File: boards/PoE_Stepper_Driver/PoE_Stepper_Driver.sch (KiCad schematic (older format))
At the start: 28 parts, among them SW3 SW_Push, U3 STM32F407VETx, U4 NCP1117, U5 E48SC12010, Y1 8MHz

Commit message: fixed ground issue
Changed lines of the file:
@@
 NoConn ~ 3225 5800
 NoConn ~ 5025 1600
-$Comp
-L ECE445:E48SC12010 U5
-U 1 1 62597F21
-P 9150 2175
-F 0 "U5" H 9475 2340 50  0000 C CNN
-F 1 "E48SC12010" H 9475 2249 50  0000 C CNN
-F 2 "PoE_Stepper_Driver:E48SC12010" H 9150 2175 50  0001 C CNN
-F 3 "" H 9150 2175 50  0001 C CNN
-	1    9150 2175
-	1    0    0    -1
-$EndComp
 Wire Wire Line
 	10050 2275 10075 2275
@@
 	10125 2275 10125 2250
 Connection ~ 10075 2275
+$Comp
+L ECE445:E48SC12010 U5
+U 1 1 62D0E6E4
+P 9150 2175
+F 0 "U5" H 9550 2340 50  0000 C CNN
+F 1 "E48SC12010" H 9550 2249 50  0000 C CNN
+F 2 "PoE_Stepper_Driver:E48SC12010" H 9150 2175 50  0001 C CNN
+F 3 "" H 9150 2175 50  0001 C CNN
+	1    9150 2175
+	1    0    0    -1
+$EndComp
 $EndSCHEMATC

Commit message: finished footprint assignment
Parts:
- removed C40: 2.2uF, symbol device:C_Small
- removed C41, C42: 2.2nF, symbol device:C_Small
- removed FL1: 1.32mH, symbol device:EMI_Filter_CommonMode
- C12, C6: value C_Small -> 20pF; footprint (none) -> Capacitor_SMD:C_0603_1608Metric_Pad1.05x0.95mm_HandSolder
- C40: renamed from C43; value 100uF -> 47uF; footprint (none) -> Capacitor_THT:CP_Radial_D8.0mm_P3.50mm
- C8, C9: footprint (none) -> Capacitor_SMD:CP_Elec_6.3x5.4
- R1, R2, R37: footprint (none) -> Resistor_SMD:R_0805_2012Metric_Pad1.15x1.40mm_HandSolder
- R3: value R_Small -> 220; footprint (none) -> Resistor_SMD:R_0603_1608Metric_Pad1.05x0.95mm_HandSolder
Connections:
- wire segments 135 -> 123
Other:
- moved on the sheet: C40, U5
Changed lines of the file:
@@
 F1 "Motor_Control.sch" 50
 $EndSheet
-Text GLabel 9050 2575 0    50   Input ~ 0
+Text GLabel 8375 2500 0    50   Input ~ 0
 PWRGD
-Text GLabel 6925 2475 0    50   Input ~ 0
+Text GLabel 7850 2275 0    50   Input ~ 0
 VOUT+
-Text GLabel 6925 2675 0    50   Input ~ 0
+Text GLabel 7850 2725 0    50   Input ~ 0
 VOUT-
 $Comp
@@
 L power:+12V #PWR014
 U 1 1 62158186
-P 10125 2250
-F 0 "#PWR014" H 10125 2100 50  0001 C CNN
-F 1 "+12V" H 10140 2423 50  0000 C CNN
-F 2 "" H 10125 2250 50  0001 C CNN
-F 3 "" H 10125 2250 50  0001 C CNN
-	1    10125 2250
+P 9450 2175
+F 0 "#PWR014" H 9450 2025 50  0001 C CNN
+F 1 "+12V" H 9465 2348 50  0000 C CNN
+F 2 "" H 9450 2175 50  0001 C CNN
+F 3 "" H 9450 2175 50  0001 C CNN
+	1    9450 2175
 	1    0    0    -1
 $EndComp
@@
 L power:GND #PWR015
 U 1 1 6215A31C
-P 10125 2900
-F 0 "#PWR015" H 10125 2650 50  0001 C CNN
-F 1 "GND" H 10130 2727 50  0000 C CNN
-F 2 "" H 10125 2900 50  0001 C CNN
-F 3 "" H 10125 2900 50  0001 C CNN
-	1    10125 2900
+P 9450 2825
+F 0 "#PWR015" H 9450 2575 50  0001 C CNN
+F 1 "GND" H 9455 2652 50  0000 C CNN
+F 2 "" H 9450 2825 50  0001 C CNN
+F 3 "" H 9450 2825 50  0001 C CNN
+	1    9450 2825
 	1    0    0    -1
 $EndComp
@@
 F 0 "C9" H 9091 4171 50  0000 L CNN
 F 1 "10uF" H 9091 4080 50  0000 L CNN
-F 2 "" H 9000 4125 50  0001 C CNN
+F 2 "Capacitor_SMD:CP_Elec_6.3x5.4" H 9000 4125 50  0001 C CNN
 F 3 "~" H 9000 4125 50  0001 C CNN
 	1    9000 4125
@@
 F 0 "C8" H 7875 4150 50  0000 L CNN
 F 1 "10uF" H 7800 4075 50  0000 L CNN
-F 2 "" H 8075 4125 50  0001 C CNN
+F 2 "Capacitor_SMD:CP_Elec_6.3x5.4" H 8075 4125 50  0001 C CNN
 F 3 "~" H 8075 4125 50  0001 C CNN
 	1    8075 4125
 	1    0    0    -1
 $EndComp
-Text Notes 8400 2125 0    50   ~ 10
+Text Notes 7725 2050 0    50   ~ 10
 Power
 $Comp
@@
 P 3000 3000
 F 0 "R3" V 3100 3000 50  0000 C CNN
-F 1 "R_Small" V 3175 3000 50  0000 C CNN
-F 2 "" H 3000 3000 50  0001 C CNN
+F 1 "220" V 3175 3000 50  0000 C CNN
+F 2 "Resistor_SMD:R_0603_1608Metric_Pad1.05x0.95mm_HandSolder" H 3000 3000 50  0001 C CNN
 F 3 "~" H 3000 3000 50  0001 C CNN
 	1    3000 3000
@@
 P 2525 2725
 F 0 "C12" V 2296 2725 50  0000 C CNN
-F 1 "C_Small" V 2387 2725 50  0000 C CNN
-F 2 "" H 2525 2725 50  0001 C CNN
+F 1 "20pF" V 2387 2725 50  0000 C CNN
+F 2 "Capacitor_SMD:C_0603_1608Metric_Pad1.05x0.95mm_HandSolder" H 2525 2725 50  0001 C CNN
 F 3 "~" H 2525 2725 50  0001 C CNN
 	1    2525 2725
@@
 P 2525 3000
 F 0 "C6" V 2650 3000 50  0000 C CNN
-F 1 "C_Small" V 2725 3000 50  0000 C CNN
-F 2 "" H 2525 3000 50  0001 C CNN
+F 1 "20pF" V 2725 3000 50  0000 C CNN
+F 2 "Capacitor_SMD:C_0603_1608Metric_Pad1.05x0.95mm_HandSolder" H 2525 3000 50  0001 C CNN
 F 3 "~" H 2525 3000 50  0001 C CNN
 	1    2525 3000
@@
 F 0 "R1" V 2404 4875 50  0000 C CNN
 F 1 "470" V 2495 4875 50  0000 C CNN
-F 2 "" H 2600 4875 50  0001 C CNN
+F 2 "Resistor_SMD:R_0805_2012Metric_Pad1.15x1.40mm_HandSolder" H 2600 4875 50  0001 C CNN
 F 3 "~" H 2600 4875 50  0001 C CNN
 	1    2600 4875
@@
 F 0 "R2" V 2675 5050 50  0000 C CNN
 F 1 "470" V 2750 5050 50  0000 C CNN
-F 2 "" H 2600 5050 50  0001 C CNN
+F 2 "Resistor_SMD:R_0805_2012Metric_Pad1.15x1.40mm_HandSolder" H 2600 5050 50  0001 C CNN
 F 3 "~" H 2600 5050 50  0001 C CNN
 	1    2600 5050
@@
 F 0 "R37" H 1534 1446 50  0000 L CNN
 F 1 "10k" H 1534 1355 50  0000 L CNN
-F 2 "" H 1475 1400 50  0001 C CNN
+F 2 "Resistor_SMD:R_0805_2012Metric_Pad1.15x1.40mm_HandSolder" H 1475 1400 50  0001 C CNN
 F 3 "~" H 1475 1400 50  0001 C CNN
 	1    1475 1400
@@
 NoConn ~ 5025 1600
 Wire Wire Line
-	10050 2275 10075 2275
-Wire Wire Line
-	10075 2275 10075 2425
-Wire Wire Line
-	10075 2425 10050 2425
-Wire Wire Line
-	10050 2725 10075 2725
-Wire Wire Line
-	10075 2725 10075 2875
-Wire Wire Line
-	10075 2875 10050 2875
-NoConn ~ 10050 2575
-$Comp
-L device:EMI_Filter_CommonMode FL1
-U 1 1 625A9D3E
-P 7525 2575
-F 0 "FL1" H 7525 2856 50  0000 C CNN
-F 1 "1.32mH" H 7525 2765 50  0000 C CNN
-F 2 "" V 7525 2615 50  0001 C CNN
-F 3 "~" V 7525 2615 50  0000 C CNN
-	1    7525 2575
-	1    0    0    -1
-$EndComp
-$Comp
-L device:C_Small C40
-U 1 1 625AEA35
-P 7200 2575
-F 0 "C40" H 7000 2625 50  0000 L CNN
-F 1 "2.2uF" H 6925 2550 50  0000 L CNN
-F 2 "" H 7200 2575 50  0001 C CNN
-F 3 "~" H 7200 2575 50  0001 C CNN
-	1    7200 2575
-	1    0    0    -1
-$EndComp
-Wire Wire Line
-	7200 2475 7325 2475
-Wire Wire Line
-	7200 2675 7325 2675
-$Comp
-L device:C_Small C41
-U 1 1 625CD945
-P 8075 2450
-F 0 "C41" H 7875 2500 50  0000 L CNN
-F 1 "2.2nF" H 7775 2400 50  0000 L CNN
-F 2 "" H 8075 2450 50  0001 C CNN
-F 3 "~" H 8075 2450 50  0001 C CNN
-	1    8075 2450
-	1    0    0    -1
-$EndComp
-$Comp
-L device:C_Small C42
-U 1 1 625D170A
-P 8075 2700
-F 0 "C42" H 7875 2750 50  0000 L CNN
-F 1 "2.2nF" H 7775 2650 50  0000 L CNN
-F 2 "" H 8075 2700 50  0001 C CNN
-F 3 "~" H 8075 2700 50  0001 C CNN
-	1    8075 2700
-	1    0    0    -1
-$EndComp
-$Comp
-L device:CP1_Small C43
+	9375 2200 9400 2200
+Wire Wire Line
+	9400 2200 9400 2350
+Wire Wire Line
+	9400 2350 9375 2350
+Wire Wire Line
+	9375 2650 9400 2650
+Wire Wire Line
+	9400 2650 9400 2800
+Wire Wire Line
+	9400 2800 9375 2800
+NoConn ~ 9375 2500
+$Comp
+L device:CP1_Small C40
 U 1 1 6260860A
-P 8600 2575
-F 0 "C43" H 8375 2625 50  0000 L CNN
-F 1 "100uF" H 8300 2525 50  0000 L CNN
-F 2 "" H 8600 2575 50  0001 C CNN
-F 3 "~" H 8600 2575 50  0001 C CNN
-	1    8600 2575
-	1    0    0    -1
-$EndComp
-$Comp
-L power:GND #PWR054
-U 1 1 6262725E
-P 8225 2850
-F 0 "#PWR054" H 8225 2600 50  0001 C CNN
-F 1 "GND" H 8225 2700 50  0000 C CNN
-F 2 "" H 8225 2850 50  0001 C CNN
-F 3 "" H 8225 2850 50  0001 C CNN
-	1    8225 2850
-	1    0    0    -1
-$EndComp
-Wire Wire Line
-	8075 2550 8075 2575
-Wire Wire Line
-	8075 2575 8225 2575
-Wire Wire Line
-	8225 2575 8225 2850
-Connection ~ 8075 2575
-Wire Wire Line
-	8075 2575 8075 2600
-Wire Wire Line
-	8075 2350 7725 2350
-Wire Wire Line
-	7725 2350 7725 2475
-Wire Wire Line
-	7725 2675 7725 2800
-Wire Wire Line
-	7725 2800 8075 2800
-Wire Wire Line
-	6925 2475 7200 2475
-Connection ~ 7200 2475
-Wire Wire Line
-	6925 2675 7200 2675
-Connection ~ 7200 2675
-Wire Wire Line
-	8075 2350 8600 2350
-Wire Wire Line
-	8600 2350 8600 2475
-Connection ~ 8075 2350
-Wire Wire Line
-	8075 2800 8600 2800
-Wire Wire Line
-	8600 2800 8600 2675
-Connection ~ 8075 2800
-Wire Wire Line
-	8600 2350 9000 2350
-Wire Wire Line
-	9000 2350 9000 2425
-Wire Wire Line
-	9000 2425 9050 2425
-Connection ~ 8600 2350
-Wire Wire Line
-	8600 2800 9000 2800
-Wire Wire Line
-	9000 2800 9000 2725
-Wire Wire Line
-	9000 2725 9050 2725
-Connection ~ 8600 2800
-Wire Wire Line
-	10075 2875 10125 2875
-Wire Wire Line
-	10125 2875 10125 2900
-Connection ~ 10075 2875
-Wire Wire Line
-	10075 2275 10125 2275
-Wire Wire Line
-	10125 2275 10125 2250
-Connection ~ 10075 2275
+P 7925 2500
+F 0 "C40" H 7700 2550 50  0000 L CNN
+F 1 "47uF" H 7625 2450 50  0000 L CNN
+F 2 "Capacitor_THT:CP_Radial_D8.0mm_P3.50mm" H 7925 2500 50  0001 C CNN
+F 3 "~" H 7925 2500 50  0001 C CNN
+	1    7925 2500
+	1    0    0    -1
+$EndComp
+Wire Wire Line
+	7925 2275 7925 2400
+Wire Wire Line
+	7925 2725 7925 2600
+Wire Wire Line
+	8325 2275 8325 2350
+Wire Wire Line
+	8325 2350 8375 2350
+Wire Wire Line
+	8325 2725 8325 2650
+Wire Wire Line
+	8325 2650 8375 2650
+Wire Wire Line
+	9400 2800 9450 2800
+Wire Wire Line
+	9450 2800 9450 2825
+Connection ~ 9400 2800
+Wire Wire Line
+	9400 2200 9450 2200
+Wire Wire Line
+	9450 2200 9450 2175
+Connection ~ 9400 2200
 $Comp
 L ECE445:E48SC12010 U5
 U 1 1 62D0E6E4
-P 9150 2175
-F 0 "U5" H 9550 2340 50  0000 C CNN
-F 1 "E48SC12010" H 9550 2249 50  0000 C CNN
-F 2 "PoE_Stepper_Driver:E48SC12010" H 9150 2175 50  0001 C CNN
-F 3 "" H 9150 2175 50  0001 C CNN
-	1    9150 2175
-	1    0    0    -1
-$EndComp
+P 8475 2100
+F 0 "U5" H 8875 2265 50  0000 C CNN
+F 1 "E48SC12010" H 8875 2174 50  0000 C CNN
+F 2 "PoE_Stepper_Driver:E48SC12010" H 8475 2100 50  0001 C CNN
+F 3 "" H 8475 2100 50  0001 C CNN
+	1    8475 2100
+	1    0    0    -1
+$EndComp
+Wire Wire Line
+	7850 2275 7925 2275
+Connection ~ 7925 2275
+Wire Wire Line
+	7925 2275 8325 2275
+Wire Wire Line
+	7850 2725 7925 2725
+Connection ~ 7925 2725
+Wire Wire Line
+	7925 2725 8325 2725
 $EndSCHEMATC

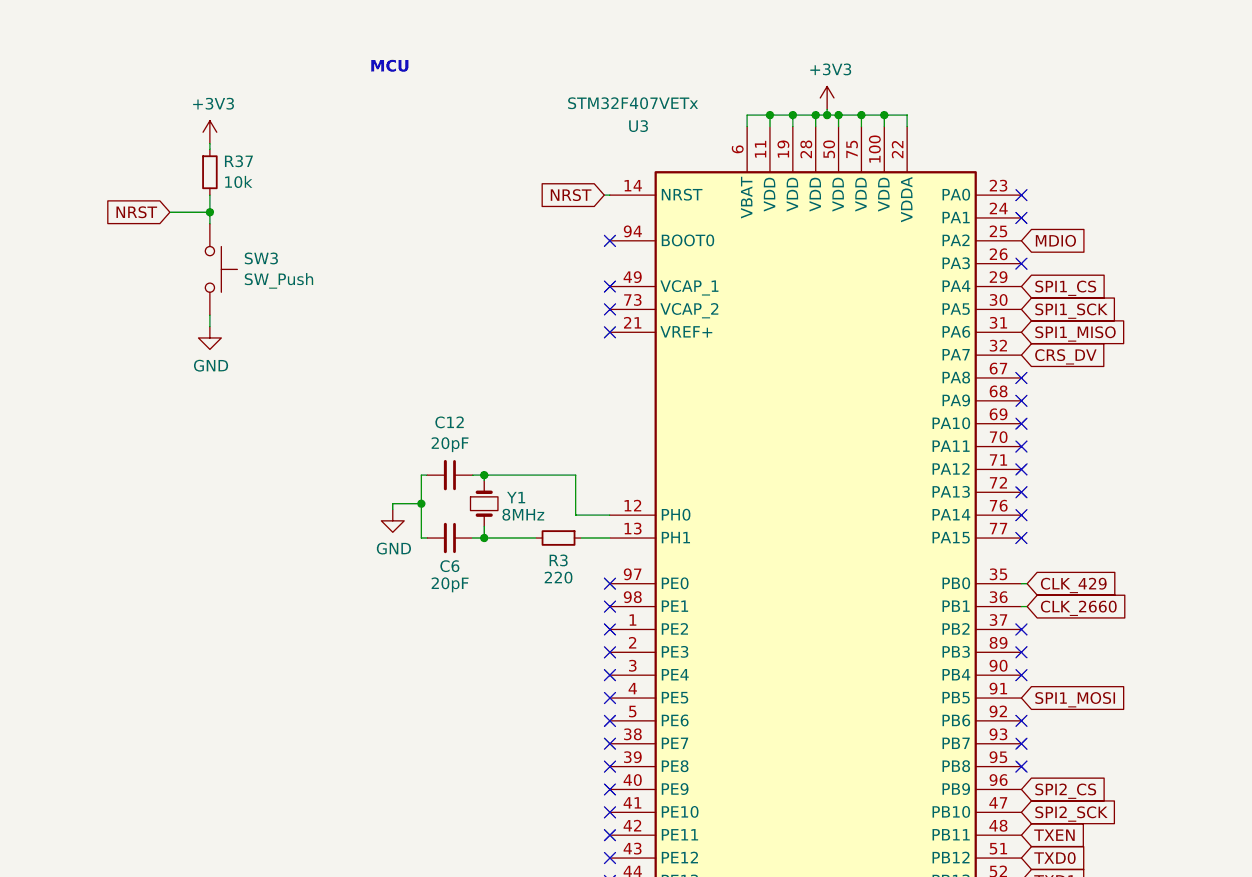
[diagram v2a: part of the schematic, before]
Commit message: added programming pins
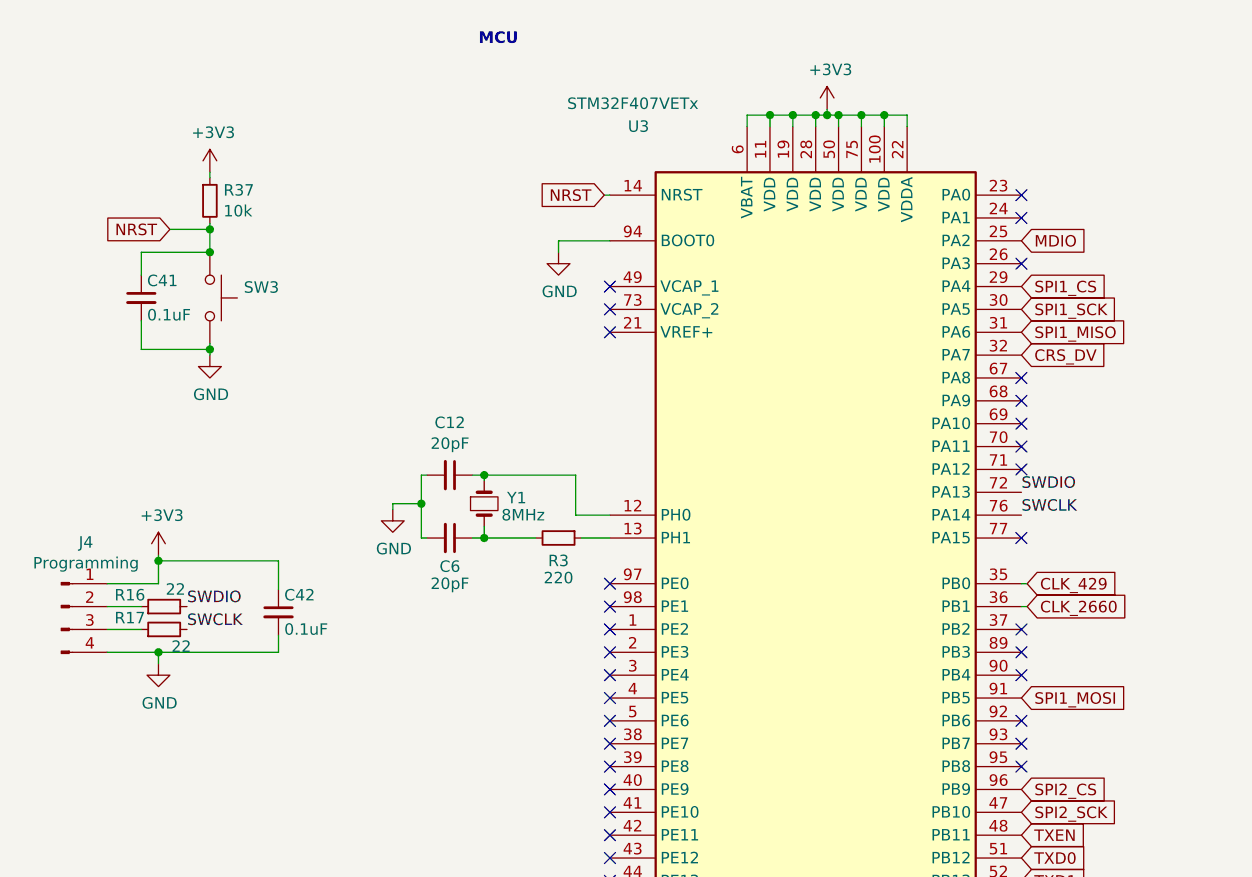
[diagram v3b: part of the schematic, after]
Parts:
- added C41, C42: 0.1uF, Capacitor_SMD:C_0805_2012Metric_Pad1.15x1.40mm_HandSolder, symbol device:C_Small
- added J4: Programming, symbol Connector:Conn_01x04_Male
- added R16, R17: 22, symbol device:R_Small
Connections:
- net +3V3: now also C42.1, J4.1 (Pin_1)
- net GND: now also U3.94 (BOOT0), C41.2, C42.2, J4.4 (Pin_4)
- net NRST: now also C41.1
- net SWDIO: now reaches U3.72 (PA13)
- net SWDIO: now also R16.2
- net SWCLK: now reaches U3.76 (PA14)
- net SWCLK: now also R17.2
- new net: J4.3 (Pin_3), R17.1
- new net: J4.2 (Pin_2), R16.1
- no-connect marks 65 -> 62
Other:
- moved on the sheet: R37, SW3
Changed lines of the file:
@@
 Text GLabel 5025 5100 2    50   Input ~ 0
 SPI2_MISO
-Text Notes 2175 975  0    50   ~ 10
+Text Notes 2650 850  0    50   ~ 10
 MCU
 $Comp
@@
 	7875 1200 7600 1200
 Connection ~ 7600 1200
-NoConn ~ 3225 1700
 NoConn ~ 3225 1900
 NoConn ~ 3225 2000
 NoConn ~ 3225 2100
-Text GLabel 1300 1575 0    50   Input ~ 0
+Text GLabel 1300 1650 0    50   Input ~ 0
 NRST
 $Comp
 L Switch:SW_Push SW3
 U 1 1 6220C2A7
-P 1475 1825
-F 0 "SW3" V 1429 1973 50  0000 L CNN
-F 1 "SW_Push" V 1520 1973 50  0000 L CNN
-F 2 "Button_Switch_SMD:SW_SPST_B3S-1000" H 1475 2025 50  0001 C CNN
-F 3 "" H 1475 2025 50  0001 C CNN
-	1    1475 1825
+P 1475 1950
+F 0 "SW3" V 1429 2098 50  0000 L CNN
+F 1 "SW_Push" V 1520 2098 50  0001 L CNN
+F 2 "Button_Switch_SMD:SW_SPST_B3S-1000" H 1475 2150 50  0001 C CNN
+F 3 "" H 1475 2150 50  0001 C CNN
+	1    1475 1950
 	0    1    1    0
 $EndComp
@@
 L power:GND #PWR052
 U 1 1 6221BC43
-P 1475 2075
-F 0 "#PWR052" H 1475 1825 50  0001 C CNN
-F 1 "GND" H 1480 1902 50  0000 C CNN
-F 2 "" H 1475 2075 50  0001 C CNN
-F 3 "" H 1475 2075 50  0001 C CNN
-	1    1475 2075
-	1    0    0    -1
-$EndComp
-Wire Wire Line
-	1475 2025 1475 2075
-Wire Wire Line
-	1300 1575 1475 1575
-Wire Wire Line
-	1475 1575 1475 1625
+P 1475 2200
+F 0 "#PWR052" H 1475 1950 50  0001 C CNN
+F 1 "GND" H 1480 2027 50  0000 C CNN
+F 2 "" H 1475 2200 50  0001 C CNN
+F 3 "" H 1475 2200 50  0001 C CNN
+	1    1475 2200
+	1    0    0    -1
+$EndComp
 $Comp
 L device:R_Small R37
 U 1 1 6222319E
-P 1475 1400
-F 0 "R37" H 1534 1446 50  0000 L CNN
-F 1 "10k" H 1534 1355 50  0000 L CNN
-F 2 "Resistor_SMD:R_0805_2012Metric_Pad1.15x1.40mm_HandSolder" H 1475 1400 50  0001 C CNN
-F 3 "~" H 1475 1400 50  0001 C CNN
-	1    1475 1400
-	1    0    0    -1
-$EndComp
-Wire Wire Line
-	1475 1500 1475 1575
-Connection ~ 1475 1575
+P 1475 1525
+F 0 "R37" H 1534 1571 50  0000 L CNN
+F 1 "10k" H 1534 1480 50  0000 L CNN
+F 2 "Resistor_SMD:R_0805_2012Metric_Pad1.15x1.40mm_HandSolder" H 1475 1525 50  0001 C CNN
+F 3 "~" H 1475 1525 50  0001 C CNN
+	1    1475 1525
+	1    0    0    -1
+$EndComp
 $Comp
 L power:+3V3 #PWR051
 U 1 1 6222741B
-P 1475 1275
-F 0 "#PWR051" H 1475 1125 50  0001 C CNN
-F 1 "+3V3" H 1490 1448 50  0000 C CNN
-F 2 "" H 1475 1275 50  0001 C CNN
-F 3 "" H 1475 1275 50  0001 C CNN
-	1    1475 1275
-	1    0    0    -1
-$EndComp
-Wire Wire Line
-	1475 1275 1475 1300
+P 1475 1400
+F 0 "#PWR051" H 1475 1250 50  0001 C CNN
+F 1 "+3V3" H 1490 1573 50  0000 C CNN
+F 2 "" H 1475 1400 50  0001 C CNN
+F 3 "" H 1475 1400 50  0001 C CNN
+	1    1475 1400
+	1    0    0    -1
+$EndComp
+Wire Wire Line
+	1475 1400 1475 1425
 NoConn ~ 3225 3200
 NoConn ~ 3225 3300
@@
 NoConn ~ 5025 2600
 NoConn ~ 5025 2700
-NoConn ~ 5025 2800
-NoConn ~ 5025 2900
 NoConn ~ 5025 3000
 NoConn ~ 5025 3400
@@
 Wire Wire Line
 	7925 2725 8325 2725
+$Comp
+L device:R_Small R17
+U 1 1 625BA2D6
+P 1275 3400
+F 0 "R17" V 1325 3550 50  0000 C CNN
+F 1 "22" V 1200 3325 50  0000 C CNN
+F 2 "" H 1275 3400 50  0001 C CNN
+F 3 "~" H 1275 3400 50  0001 C CNN
+	1    1275 3400
+	0    -1   -1   0
+$EndComp
+$Comp
+L power:GND #PWR056
+U 1 1 625BB5F0
+P 3000 1750
+F 0 "#PWR056" H 3000 1500 50  0001 C CNN
+F 1 "GND" H 3005 1577 50  0000 C CNN
+F 2 "" H 3000 1750 50  0001 C CNN
+F 3 "" H 3000 1750 50  0001 C CNN
+	1    3000 1750
+	1    0    0    -1
+$EndComp
+Wire Wire Line
+	3225 1700 3000 1700
+Wire Wire Line
+	3000 1700 3000 1750
+$Comp
+L Connector:Conn_01x04_Male J4
+U 1 1 625C4DFF
+P 825 3300
+F 0 "J4" H 933 3581 50  0000 C CNN
+F 1 "Programming" H 933 3490 50  0000 C CNN
+F 2 "" H 825 3300 50  0001 C CNN
+F 3 "~" H 825 3300 50  0001 C CNN
+	1    825  3300
+	1    0    0    -1
+$EndComp
+Wire Wire Line
+	1025 3400 1175 3400
+$Comp
+L device:R_Small R16
+U 1 1 625DA239
+P 1275 3300
+F 0 "R16" V 1325 3450 50  0000 C CNN
+F 1 "22" V 1350 3250 50  0000 C CNN
+F 2 "" H 1275 3300 50  0001 C CNN
+F 3 "~" H 1275 3300 50  0001 C CNN
+	1    1275 3300
+	0    -1   -1   0
+$EndComp
+Wire Wire Line
+	1025 3300 1175 3300
+Text Label 1375 3300 0    50   ~ 0
+SWDIO
+Wire Wire Line
+	1025 3200 1250 3200
+Wire Wire Line
+	1250 3200 1250 3100
+$Comp
+L power:GND #PWR055
+U 1 1 625F67DF
+P 1250 3550
+F 0 "#PWR055" H 1250 3300 50  0001 C CNN
+F 1 "GND" H 1255 3377 50  0000 C CNN
+F 2 "" H 1250 3550 50  0001 C CNN
+F 3 "" H 1250 3550 50  0001 C CNN
+	1    1250 3550
+	1    0    0    -1
+$EndComp
+Wire Wire Line
+	1025 3500 1250 3500
+Wire Wire Line
+	1250 3500 1250 3550
+Text Label 1375 3400 0    50   ~ 0
+SWCLK
+Text Label 5025 2800 0    50   ~ 0
+SWDIO
+Text Label 5025 2900 0    50   ~ 0
+SWCLK
+$Comp
+L device:C_Small C42
+U 1 1 626271EE
+P 1775 3325
+F 0 "C42" H 1800 3400 50  0000 L CNN
+F 1 "0.1uF" H 1800 3250 50  0000 L CNN
+F 2 "Capacitor_SMD:C_0805_2012Metric_Pad1.15x1.40mm_HandSolder" H 1775 3325 50  0001 C CNN
+F 3 "~" H 1775 3325 50  0001 C CNN
+	1    1775 3325
+	1    0    0    -1
+$EndComp
+$Comp
+L power:+3V3 #PWR054
+U 1 1 625F1239
+P 1250 3075
+F 0 "#PWR054" H 1250 2925 50  0001 C CNN
+F 1 "+3V3" H 1265 3248 50  0000 C CNN
+F 2 "" H 1250 3075 50  0001 C CNN
+F 3 "" H 1250 3075 50  0001 C CNN
+	1    1250 3075
+	1    0    0    -1
+$EndComp
+Wire Wire Line
+	1250 3100 1775 3100
+Wire Wire Line
+	1775 3100 1775 3225
+Connection ~ 1250 3100
+Wire Wire Line
+	1250 3100 1250 3075
+Wire Wire Line
+	1775 3500 1250 3500
+Wire Wire Line
+	1775 3425 1775 3500
+Connection ~ 1250 3500
+$Comp
+L device:C_Small C41
+U 1 1 62641795
+P 1175 1950
+F 0 "C41" H 1200 2025 50  0000 L CNN
+F 1 "0.1uF" H 1200 1875 50  0000 L CNN
+F 2 "Capacitor_SMD:C_0805_2012Metric_Pad1.15x1.40mm_HandSolder" H 1175 1950 50  0001 C CNN
+F 3 "~" H 1175 1950 50  0001 C CNN
+	1    1175 1950
+	1    0    0    -1
+$EndComp
+Wire Wire Line
+	1475 1625 1475 1650
+Wire Wire Line
+	1300 1650 1475 1650
+Connection ~ 1475 1650
+Wire Wire Line
+	1475 1650 1475 1750
+Wire Wire Line
+	1475 2150 1475 2175
+Wire Wire Line
+	1175 1850 1175 1750
+Wire Wire Line
+	1175 1750 1475 1750
+Connection ~ 1475 1750
+Wire Wire Line
+	1175 2050 1175 2175
+Wire Wire Line
+	1175 2175 1475 2175
+Connection ~ 1475 2175
+Wire Wire Line
+	1475 2175 1475 2200
 $EndSCHEMATC

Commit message: burhhhhh sheeeeeeeeeeeeeeeeeesh
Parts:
- C41: value 0.1uF -> 1uF
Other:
- moved on the sheet: C10, C34, C35, C36, C37, C38, C39, C40, C7, C8, C9, U4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
